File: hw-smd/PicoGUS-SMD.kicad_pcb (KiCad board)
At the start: 2 copper layers, 103.7 x 99.8 mm, 81 parts, among them J1 2x9 header, J3 Bus_ISA_8bit, J5 SJ1-3535NG (black), J6 1x40 breakaway header, J7 1x40 breakaway header, J8 SJ1-3535NG-GR (green), J9 Waveblaster 2x13 male, U1 Raspberry Pi Pico, U10 74LVC2G06, U11 NE5532, U12 74LVC2G06, U2 74LVC244, U3 SN74CB3T3257, U4 SN74CB3T3257, U5 74AHC14, U6 74LVC00, U7 74LVC1G00, U8 APS6404L-3SQR-SN, U9 PCM5100A

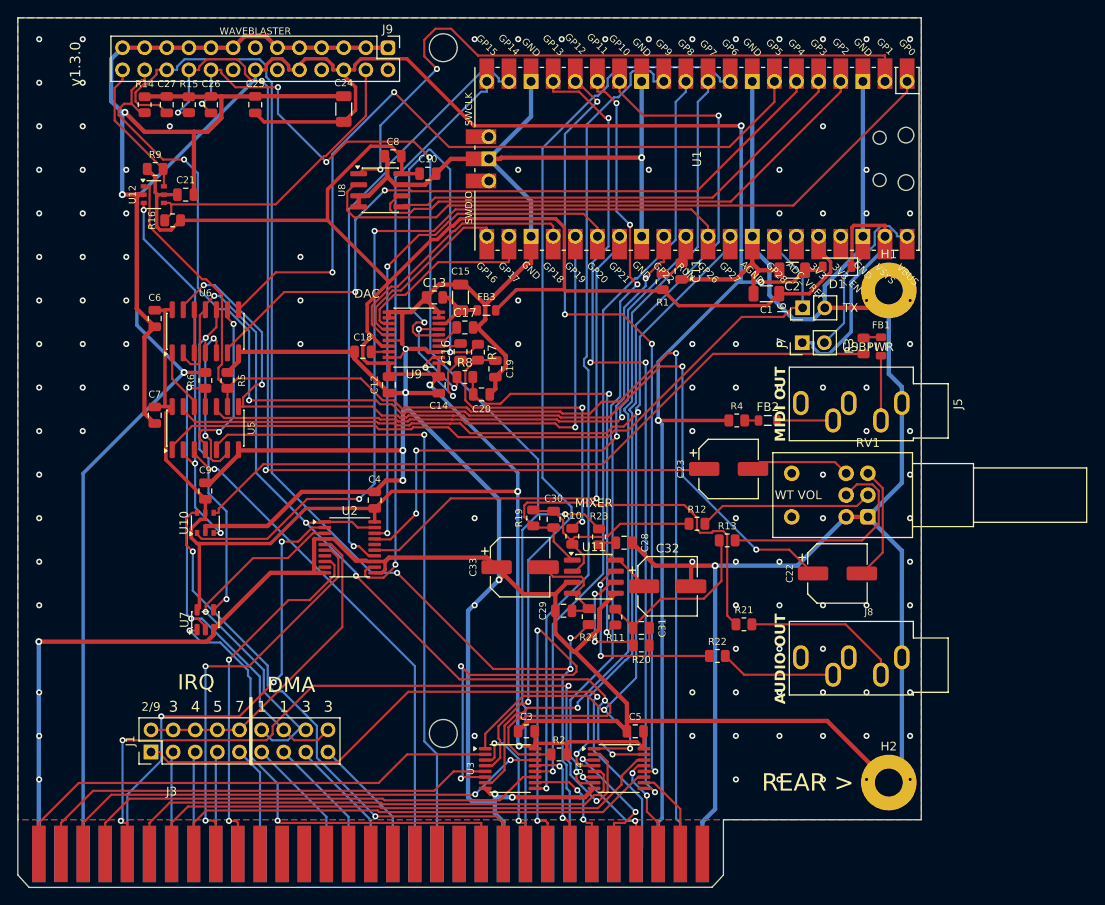
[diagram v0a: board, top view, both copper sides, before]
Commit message: hw-tht: adopt the new hand-made component placement; label clean-up
- THT board rebuilt on the uploaded layout: every part position,
  rotation and reference label kept as placed (R17 moved 0.5 mm down to
  clear C7's courtyard), texts/logo kept; fully re-routed, GND stitched,
  0 DRC errors, 0 unconnected, schematic parity OK. No schematic change
  needed: every cap/resistor sits at the pins it serves.
- Pico pin-name / SWD silkscreen texts removed (THT and SMD).
- WAVEBLASTER, DAC, MIXER and WT VOL labels in Futura bold; WT VOL now
  sits beside RV1 exactly as MIDI OUT / AUDIO OUT sit beside their jacks.
- hw-smd: same label treatment; C23 moved 1.8 mm left to clear WT VOL,
  board re-routed (0 DRC errors).

Co-Authored-By: Claude Opus 5.5 <noreply@anthropic.com>
Claude-Session: https://claude.ai/code/session_011utN3x8yYUNDvkpGCEq5yD
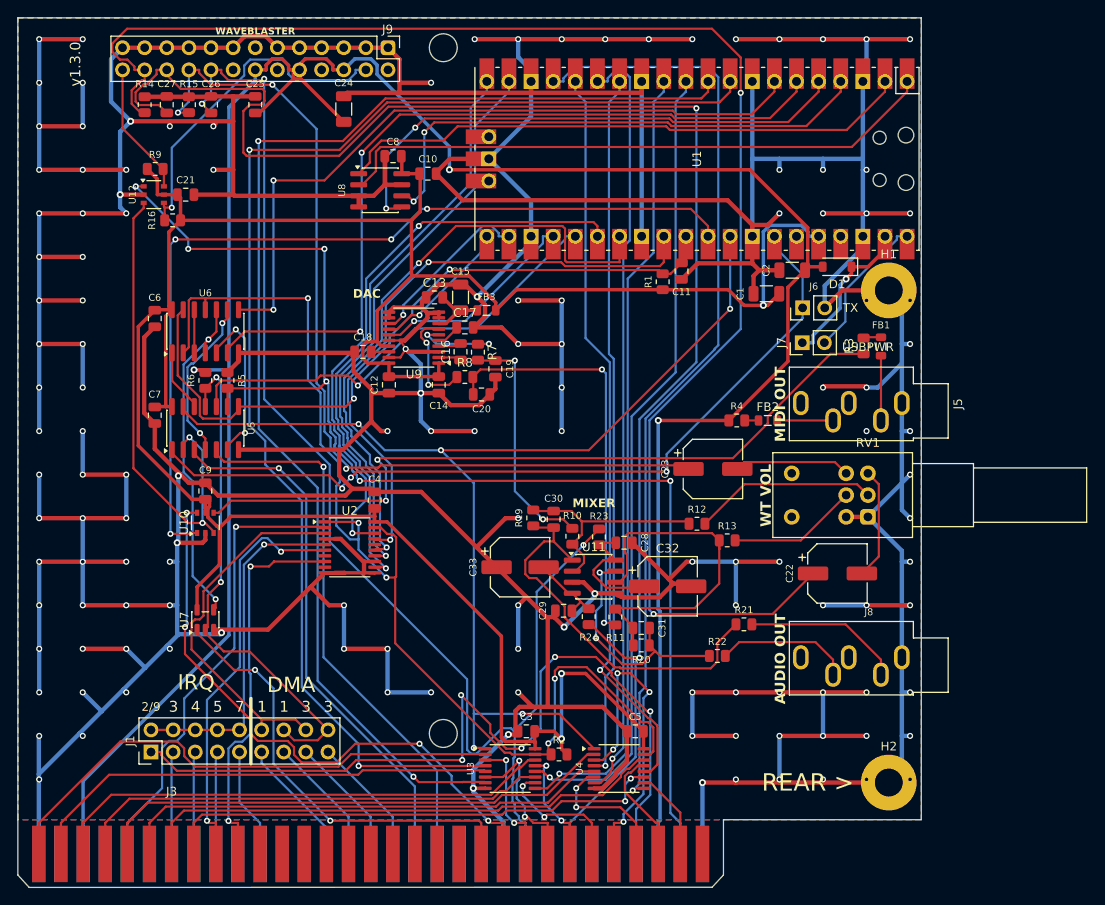
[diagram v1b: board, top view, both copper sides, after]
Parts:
- moved C23 1.80 mm to (196.2, 88.0)
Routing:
- net GND: track 816.2 -> 1246.3 mm, vias 122 -> 133
- net AD1: track 95.7 -> 144.1 mm, vias 1 -> 2
- net AD0: track 104.2 -> 149.6 mm, vias 1 -> 2
- net D1: track 63.2 -> 18.1 mm, vias 4 -> 2
- net Net-(U9-OUTL): track 54.8 -> 10.1 mm
- net -12V: track 141.5 -> 185.4 mm, vias 3 -> 2
- net /Wavetable & line out/WT_L: track 135.4 -> 175.3 mm, vias 4 -> 2
- net A4: track 89.9 -> 60.4 mm, vias 4 -> 0
- net IRQ2: track 76.3 -> 97.8 mm, vias 1 -> 5
- net D4: track 16.5 -> 37.1 mm, vias 2 -> 4
- net +3V3: track 310.6 -> 294.3 mm
- net AD4: track 97.1 -> 81.0 mm, vias 2 -> 1
- net +12V: track 132.8 -> 148.6 mm, vias 5 -> 3
- net RUN: track 97.9 -> 83.0 mm, vias 3 -> 2
- net ~{RDACK}: track 64.6 -> 51.9 mm
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
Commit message: JLCPCB export flow; hw-smd re-synced to the new THT placement
- hw-common/tools/jlcpcb.sh: DRC gate (incl. schematic parity), Gerbers
  (Protel ext., no X2) + Excellon drill zipped for upload, JLC assembly
  BOM + CPL for SMD parts.
- .github/workflows/hardware.yml: runs it for hw-tht and hw-smd in the
  kicad/kicad:10.0 container and uploads the files as artifacts.
- hw-smd: parts moved to the new hand-made THT layout (SMD part at the
  THT part's centre), decoupling caps re-seated at their own chips,
  C22/C23 re-placed next to RV1; U10 GND pre-routed to a via; fully
  re-routed, 0 DRC errors, 0 unconnected, schematic parity OK.
- READMEs: JLCPCB ordering section.

Co-Authored-By: Claude Opus 5.5 <noreply@anthropic.com>
Claude-Session: https://claude.ai/code/session_011utN3x8yYUNDvkpGCEq5yD
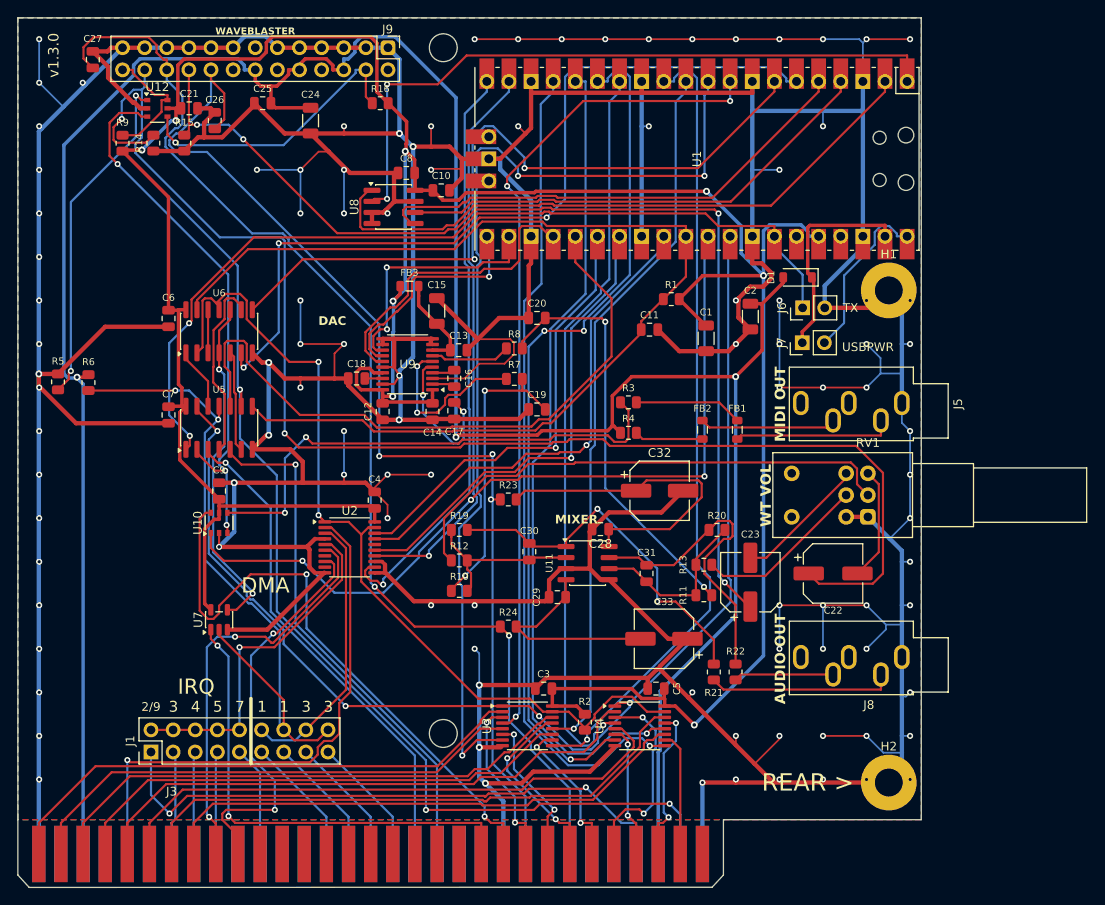
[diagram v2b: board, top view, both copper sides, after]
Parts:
- moved R3 27.8 mm to (186.5, 80.3), turned to 0 degrees
- moved R12 27.6 mm to (167.1, 98.5), turned to 0 degrees
- moved R16 27.4 mm to (158.0, 46.0)
- moved R5 19.5 mm to (121.0, 78.0)
- moved FB1 19.1 mm to (199.0, 83.5)
- moved C33 18.5 mm to (190.6, 107.5), turned to 180 degrees
- moved R20 15.8 mm to (196.7, 95.0), turned to 180 degrees
- moved R10 14.4 mm to (167.1, 102.0), turned to 0 degrees
- moved C23 13.7 mm to (200.5, 101.0), turned to 90 degrees
- moved R6 13.4 mm to (124.5, 78.1)
- moved R4 12.5 mm to (186.5, 83.8)
- moved R23 11.3 mm to (172.7, 91.5), turned to 0 degrees
- moved C32 11.0 mm to (190.1, 90.5)
- moved C20 10.8 mm to (176.0, 70.7), turned to 0 degrees
- moved R11 10.5 mm to (195.2, 102.5), turned to 180 degrees
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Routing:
- net GND: track 1246.3 -> 1093.5 mm, vias 133 -> 102
- net AD0: track 149.6 -> 96.0 mm, vias 2 -> 3
- net +3V3: track 294.3 -> 346.4 mm, vias 3 -> 8
- net -12V: track 185.4 -> 134.4 mm
- net RUN: track 83.0 -> 126.1 mm, vias 2 -> 0
- net Net-(R12-Pad1): track 21.1 -> 59.7 mm
- net ~{BUSOE}: track 131.6 -> 101.5 mm, vias 5 -> 2
- net IRQ2: track 97.8 -> 68.1 mm, vias 5 -> 2
- net AD1: track 144.1 -> 115.5 mm, vias 2 -> 3
- net Net-(R3-Pad1): track 86.8 -> 59.0 mm
- net ~{RDACK}: track 51.9 -> 76.3 mm, vias 1 -> 0
- net /Wavetable & line out/+12VA: track 14.7 -> 38.2 mm
- net +5V: track 282.0 -> 303.0 mm
- net Net-(U11B--): track 41.7 -> 20.8 mm
- net +12V: track 148.6 -> 128.2 mm
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
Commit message: Experimental 2nd IRQ (J10/J11), DMA label fix, labels grouped
- U2's spare channel (2A2 pin 13 -> 2Y2 pin 7, same drive and ~BUSOE as the
  IRQ output) now drives an optional second IRQ: J10 (next to the PSRAM,
  short stub on the fast SPI line) links GPIO3/SPI_TX to 2A2, R25 (10k)
  holds it low when open; J11 (next to J1) links 2Y2 to ISA IRQ3.
  GPIO3 is the PSRAM SPI_TX (all 26 Pico GPIOs are used), so this is for
  firmware that leaves the PSRAM idle. THT and SMD, ERC 0 errors.
- DMA heading moved back beside IRQ above J1.
- Silkscreen labels are members of their circuit-block KiCad groups
  (DAC, MIXER, AUDIO OUT, WT VOL, WAVEBLASTER, MIDI OUT, TX/USBPWR,
  IRQ/DMA + jumper numbers + divider, 2ND IRQ).
- Both boards re-routed: 0 DRC errors, 0 unconnected, schematic parity OK.
- BOMs: R25, J10/J11 (from the 1x40 strip), 6 jumper shunts.

Co-Authored-By: Claude Opus 5.5 <noreply@anthropic.com>
Claude-Session: https://claude.ai/code/session_011utN3x8yYUNDvkpGCEq5yD
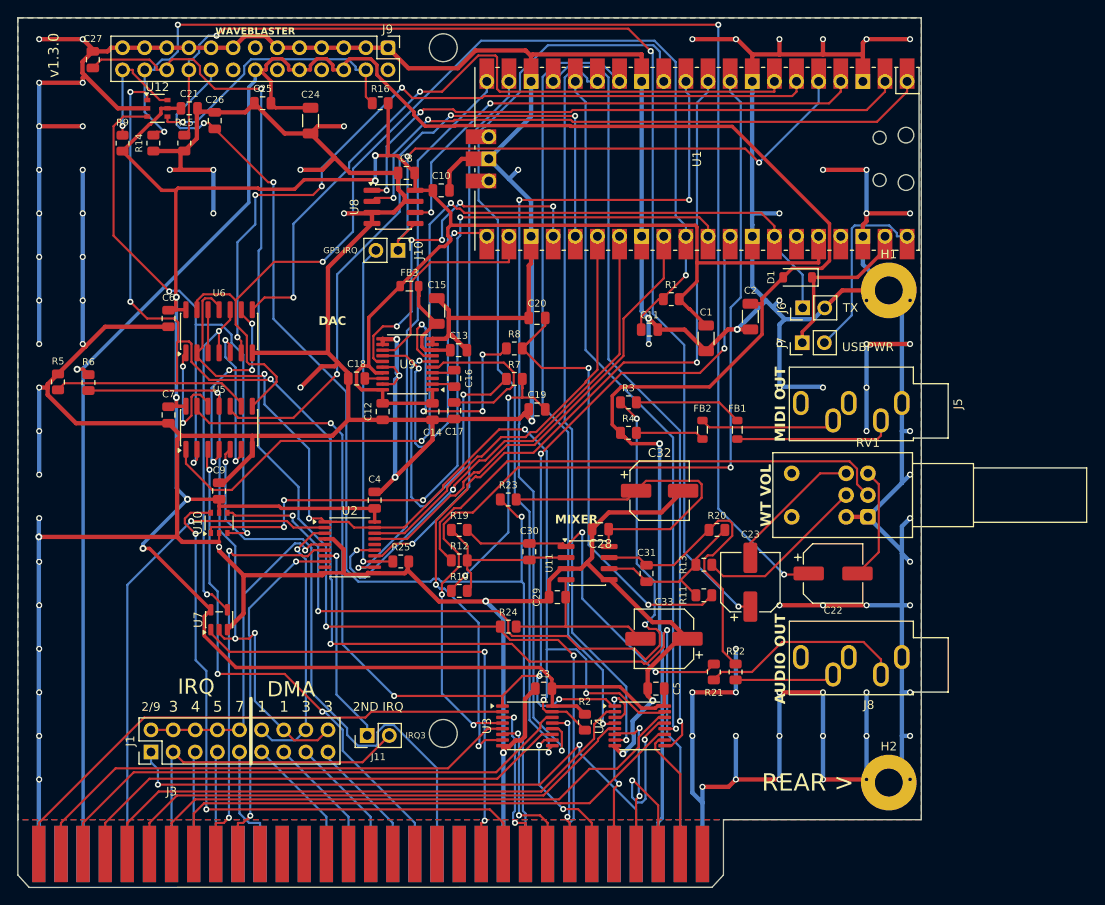
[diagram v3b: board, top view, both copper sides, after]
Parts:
- added J10: Jumper, Connector_PinHeader_2.54mm:PinHeader_1x02_P2.54mm_Vertical, F.Cu at (160.0, 62.9)
- added J11: Jumper, Connector_PinHeader_2.54mm:PinHeader_1x02_P2.54mm_Vertical, F.Cu at (156.5, 118.6)
- added R25: 10k, Resistor_SMD:R_0805_2012Metric, F.Cu at (160.4, 98.6)
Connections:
- U2 pad 13: GND -> IRQ2ND_IN
- U2 pad 7: (no net) -> IRQ2ND_OUT
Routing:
- net IRQ2ND_IN: track 0.00 -> 39.7 mm, vias 0 -> 1
- net Net-(R3-Pad1): track 59.0 -> 93.9 mm, vias 2 -> 4
- net +3V3: track 346.4 -> 314.8 mm, vias 8 -> 6
- net IRQ3: track 12.0 -> 38.4 mm
- net ~{BUSOE}: track 101.5 -> 126.5 mm, vias 2 -> 5
- net IRQ2ND_OUT: track 0.00 -> 23.4 mm, vias 0 -> 1
- net Net-(U9-OUTR): track 9.18 -> 31.7 mm, vias 0 -> 4
- net GND: track 1093.5 -> 1071.7 mm, vias 102 -> 95
- net Net-(U9-OUTL): track 19.6 -> 40.0 mm
- net AD2: track 82.1 -> 102.0 mm, vias 1 -> 3
- net DIN: track 25.9 -> 44.6 mm, vias 1 -> 2
- net +5V: track 303.0 -> 286.1 mm, vias 3 -> 2
- net ~{MIDI_DRV}: track 63.0 -> 79.8 mm
- net AD0: track 96.0 -> 110.5 mm
- net AD6: track 94.8 -> 80.4 mm
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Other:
- board text added: "2ND IRQ"
- board text added: "GP3 IRQ"
- board text added: "IRQ3"

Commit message: hw-smd: J11 vertical with NE2000/IRQ3 label, H1/H2 silk removed; re-routed (0 DRC errors, 0 unconnected)
Co-Authored-By: Claude Opus 5.5 <noreply@anthropic.com>
Claude-Session: https://claude.ai/code/session_011utN3x8yYUNDvkpGCEq5yD
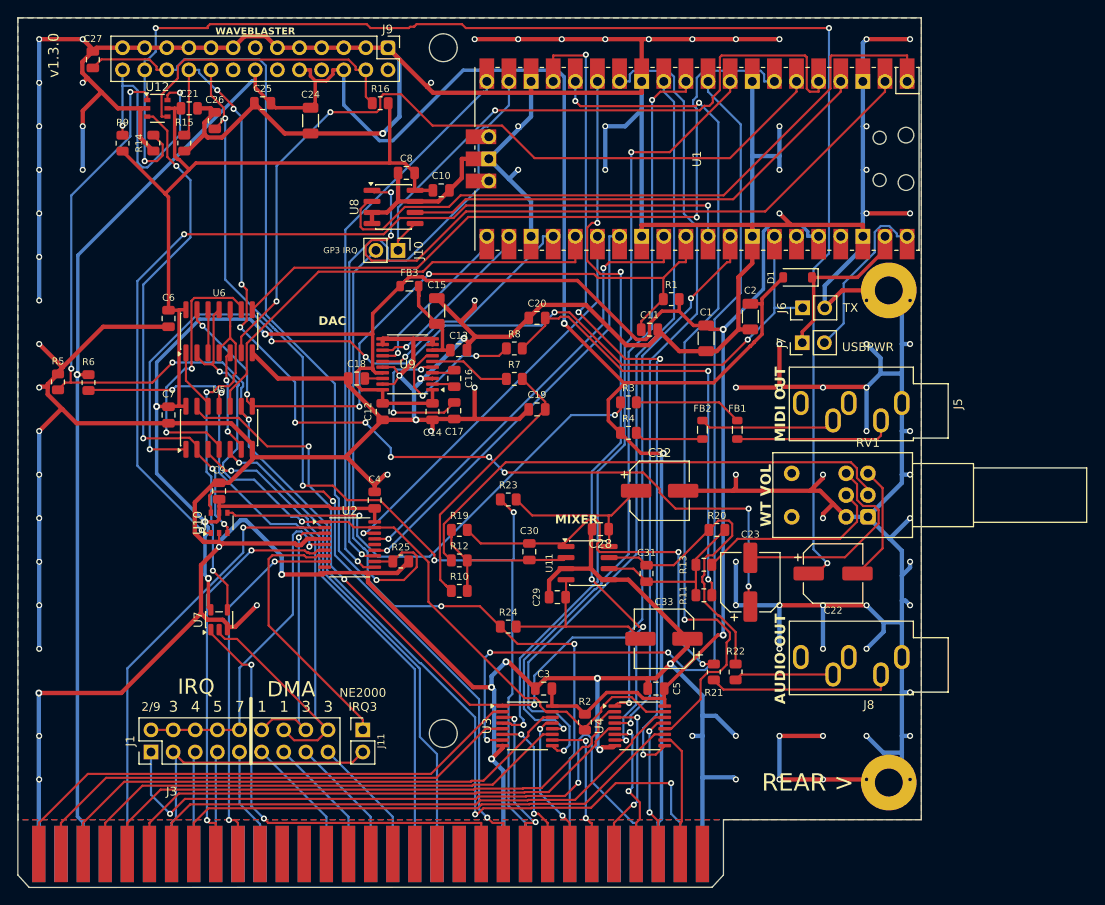
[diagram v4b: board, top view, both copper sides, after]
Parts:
- moved J11 0.81 mm to (156.0, 118.0), turned to 0 degrees
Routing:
- net RUN: track 124.1 -> 85.0 mm, vias 2 -> 4
- net Net-(R3-Pad1): track 93.9 -> 57.2 mm, vias 4 -> 2
- net ~{BUSOE}: track 126.5 -> 92.4 mm, vias 5 -> 2
- net GND: track 1071.7 -> 1103.3 mm, vias 95 -> 100
- net Net-(U9-OUTL): track 40.0 -> 9.32 mm, vias 2 -> 0
- net ~{RDACK}: track 79.2 -> 52.6 mm, vias 3 -> 0
- net DIN: track 44.6 -> 19.5 mm, vias 2 -> 1
- net AD0: track 110.5 -> 89.3 mm, vias 3 -> 2
- net RESET: track 178.4 -> 157.7 mm, vias 5 -> 6
- net ~{MIDI_DRV}: track 79.8 -> 59.7 mm, vias 3 -> 4
- net AD6: track 80.4 -> 99.9 mm, vias 1 -> 3
- net /Wavetable & line out/+12VA: track 38.1 -> 19.3 mm
- net DACK: track 69.2 -> 87.0 mm, vias 3 -> 2
- net /Wavetable & line out/~{WT_RESET}: track 14.3 -> 31.3 mm, vias 1 -> 2
- net /Wavetable & line out/WT_L: track 148.6 -> 164.8 mm
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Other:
- board text added: "NE2000 IRQ3"
- board text removed: "2ND IRQ"
- board text removed: "IRQ3"

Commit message: v1.3.0: drop the experimental 2nd IRQ; back-side artwork; label clean-up
- Experimental second IRQ removed from both boards: J10, J11 and R25 are gone,
  U2 pin 13 is tied to GND again and pin 7 is unconnected, as on v1.2.
  BOMs and DigiKey upload CSVs: one 10k less, 4 jumper shunts.
- Back silkscreen: the "Mila and Alisa" artwork (hw-common/art/mila-alisa.svg)
  with the dedication below it, mirrored so it reads from the back. On THT it
  is cut out 0.3 mm around every pad and hole, and the dedication sits in the
  one pad-free strip.
- Reference labels: U3/U4 horizontal under the chips; jumper labels J1/J6/J7
  upright; round capacitor labels (C1, C2, C22, C23, C32, C33) moved to free
  spots; the J3 (ISA fingers) label is hidden.
- Both boards: 0 DRC errors, 0 unconnected, schematic parity OK; ERC 0 errors.

Co-Authored-By: Claude Opus 5.5 <noreply@anthropic.com>
Claude-Session: https://claude.ai/code/session_011utN3x8yYUNDvkpGCEq5yD
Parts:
- removed J10, J11: Jumper, Connector_PinHeader_2.54mm:PinHeader_1x02_P2.54mm_Vertical
- removed R25: 10k, Resistor_SMD:R_0805_2012Metric
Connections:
- U2 pad 13: IRQ2ND_IN -> GND
- U2 pad 7: IRQ2ND_OUT -> (no net)
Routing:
- net IRQ2ND_IN: track 52.0 -> 0.00 mm, vias 1 -> 0
- net IRQ2ND_OUT: track 30.9 -> 0.00 mm
- net IRQ3: track 34.8 -> 12.1 mm
- net SPI_TX: vias 1 -> 2
- net GND: vias 100 -> 99
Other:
- board text added: "This version is dedicated to Mila and Alisa, my two wonderful princesses, who fill my world with joy."
- board text removed: "GP3 IRQ"
- board text removed: "NE2000 IRQ3"
